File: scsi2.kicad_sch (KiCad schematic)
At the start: 25 parts, among them J3 TO-LED, J4 TO-MB, U4 NCR53c710 SCSI Host Controller, U7 SST39SF010, Y1 Abracon ACO-50MHz

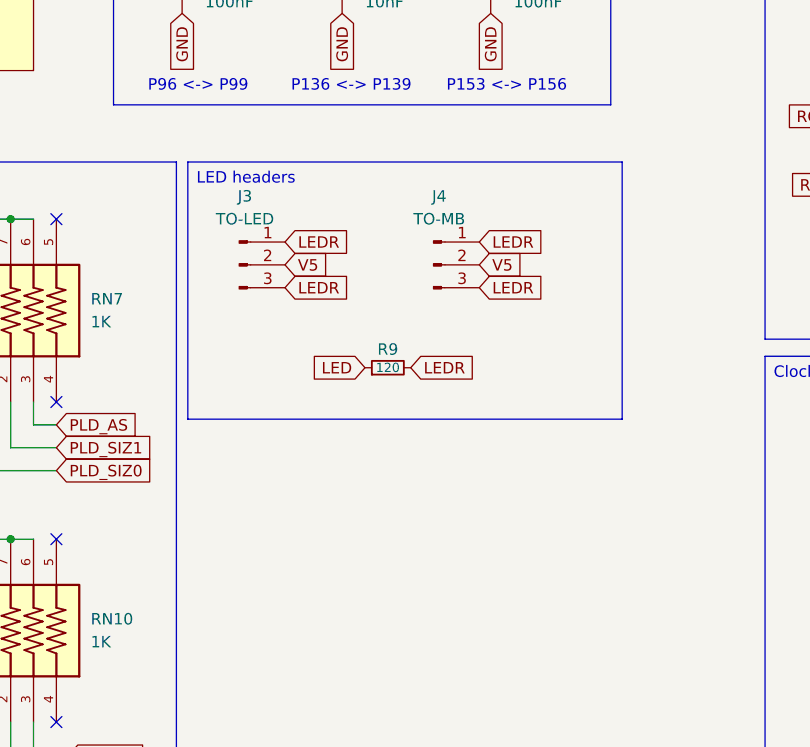
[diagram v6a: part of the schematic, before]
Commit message: Free up some pins and add an LED
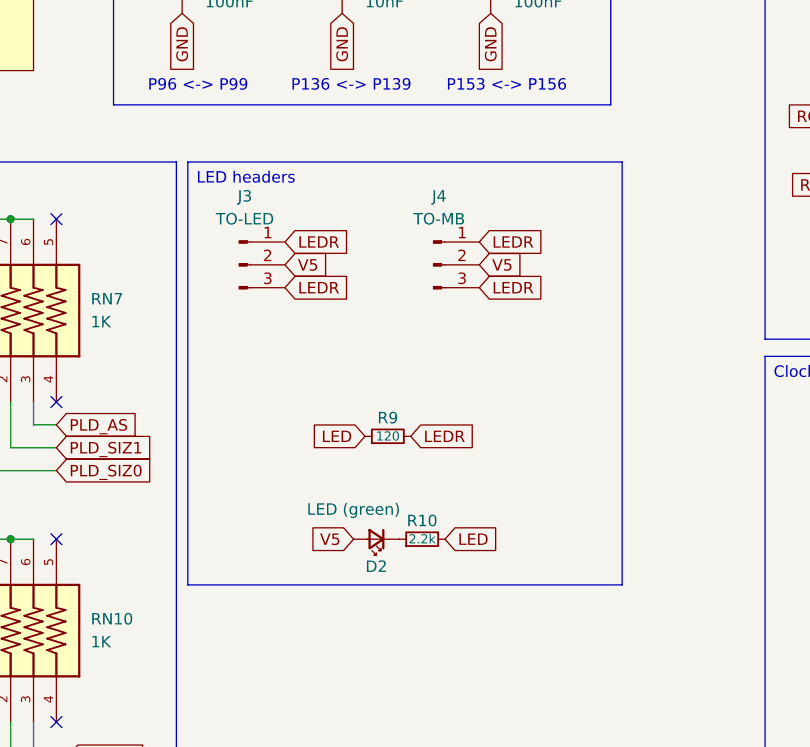
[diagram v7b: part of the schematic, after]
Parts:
- added D2: LED (green), LED_SMD:LED_0805_2012Metric, symbol Device:LED_Small
- added R10: 2.2k, Resistor_SMD:R_0603_1608Metric, symbol Device:R_Small
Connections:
- net LED: now also R10.2
- net V5: now also D2.2 (A)
- new net: D2.1 (K), R10.1
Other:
- moved on the sheet: R9
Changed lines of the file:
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@@
 		(exclude_from_sim no)
 		(at 165.735 86.36 0)
-		(size 48.26 28.575)
+		(size 48.26 46.99)
 		(margins 0.9525 0.9525 0.9525 0.9525)
 		(stroke
@@
 		)
 	)
+	(global_label "V5"
+		(shape input)
+		(at 184.15 128.27 180)
+		(fields_autoplaced yes)
+		(effects
+			(font
+				(size 1.27 1.27)
+			)
+			(justify right)
+		)
+		(property "Intersheetrefs" "${INTERSHEET_REFS}"
+			(at 178.8667 128.27 0)
+			(effects
+				(font
+					(size 1.27 1.27)
+				)
+				(justify right)
+				(hide yes)
+			)
+		)
+	)
 	(global_label "D24"
 		(shape input)
@@
 	(global_label "LEDR"
 		(shape input)
-		(at 190.5 109.22 0)
+		(at 190.5 116.84 0)
 		(fields_autoplaced yes)
 		(effects
@@
 		)
 		(property "Intersheetrefs" "${INTERSHEET_REFS}"
-			(at 198.2023 109.22 0)
+			(at 198.2023 116.84 0)
 			(effects
 				(font
@@
 	(global_label "LED"
 		(shape input)
-		(at 185.42 109.22 180)
+		(at 185.42 116.84 180)
 		(fields_autoplaced yes)
 		(effects
@@
 		)
 		(property "Intersheetrefs" "${INTERSHEET_REFS}"
-			(at 178.9877 109.22 0)
+			(at 178.9877 116.84 0)
 			(effects
 				(font
@@
 		)
 	)
+	(global_label "LED"
+		(shape input)
+		(at 194.31 128.27 0)
+		(fields_autoplaced yes)
+		(effects
+			(font
+				(size 1.27 1.27)
+			)
+			(justify left)
+		)
+		(property "Intersheetrefs" "${INTERSHEET_REFS}"
+			(at 200.7423 128.27 0)
+			(effects
+				(font
+					(size 1.27 1.27)
+				)
+				(justify left)
+				(hide yes)
+			)
+		)
+	)
 	(global_label "A28"
 		(shape input)
@@
 	)
 	(symbol
+		(lib_id "Device:LED_Small")
+		(at 186.69 128.27 180)
+		(unit 1)
+		(exclude_from_sim no)
+		(in_bom yes)
+		(on_board yes)
+		(dnp no)
+		(property "Reference" "D2"
+			(at 186.69 131.318 0)
+			(effects
+				(font
+					(size 1.27 1.27)
+				)
+			)
+		)
+		(property "Value" "LED (green)"
+			(at 184.15 124.968 0)
+			(effects
+				(font
+					(size 1.27 1.27)
+				)
+			)
+		)
+		(property "Footprint" "LED_SMD:LED_0805_2012Metric"
+			(at 186.69 128.27 90)
+			(effects
+				(font
+					(size 1.27 1.27)
+				)
+				(hide yes)
+			)
+		)
+		(property "Datasheet" "~"
+			(at 186.69 128.27 90)
+			(effects
+				(font
+					(size 1.27 1.27)
+				)
+				(hide yes)
+			)
+		)
+		(property "Description" "Light emitting diode, small symbol"
+			(at 186.69 128.27 0)
+			(effects
+				(font
+					(size 1.27 1.27)
+				)
+				(hide yes)
+			)
+		)
+		(property "Sim.Pin" "1=K 2=A"
+			(at 186.69 128.27 0)
+			(effects
+				(font
+					(size 1.27 1.27)
+				)
+				(hide yes)
+			)
+		)
+		(pin "1"
+		)
+		(pin "2"
+		)
+		(instances
+			(project "A4092"
+				(path "/8f9f4021-47aa-41d9-bea7-f6ccf72098bb/2daf4fe3-1e72-4ad5-914a-264df02f69b3"
+					(reference "D2")
+					(unit 1)
+				)
+			)
+		)
+	)
+	(symbol
 		(lib_id "Device:C_Small")
 		(at 165.1 67.31 0)
@@
 	(symbol
 		(lib_id "Device:R_Small")
-		(at 187.96 109.22 90)
+		(at 187.96 116.84 90)
 		(unit 1)
 		(exclude_from_sim no)
@@
 		(dnp no)
 		(property "Reference" "R9"
-			(at 187.96 107.188 90)
+			(at 187.96 114.808 90)
 			(effects
 				(font
@@
 		)
 		(property "Value" "120"
-			(at 187.96 109.22 90)
+			(at 187.96 116.84 90)
 			(effects
 				(font
@@
 		)
 		(property "Footprint" "Resistor_SMD:R_0603_1608Metric"
-			(at 187.96 109.22 0)
+			(at 187.96 116.84 0)
 			(effects
 				(font
@@
 		)
 		(property "Datasheet" "~"
-			(at 187.96 109.22 0)
+			(at 187.96 116.84 0)
 			(effects
 				(font
@@
 		)
 		(property "Description" "Resistor, small symbol"
-			(at 187.96 109.22 0)
+			(at 187.96 116.84 0)
 			(effects
 				(font
@@
 					(unit 1)
 				)
+			)
+		)
+	)
+	(symbol
+		(lib_id "Device:R_Small")
+		(at 191.77 128.27 90)
+		(unit 1)
+		(exclude_from_sim no)
+		(in_bom yes)
+		(on_board yes)
+		(dnp no)
+		(property "Reference" "R10"
+			(at 191.77 126.238 90)
+			(effects
+				(font
+					(size 1.27 1.27)
+				)
+			)
+		)
+		(property "Value" "2.2k"
+			(at 191.77 128.27 90)
+			(effects
+				(font
+					(size 1.016 1.016)
+				)
+			)
+		)
+		(property "Footprint" "Resistor_SMD:R_0603_1608Metric"
+			(at 191.77 128.27 0)
+			(effects
+				(font
+					(size 1.27 1.27)
+				)
+				(hide yes)
+			)
+		)
+		(property "Datasheet" "~"
+			(at 191.77 128.27 0)
+			(effects
+				(font
+					(size 1.27 1.27)
+				)
+				(hide yes)
+			)
+		)
+		(property "Description" "Resistor, small symbol"
+			(at 191.77 128.27 0)
+			(effects
+				(font
+					(size 1.27 1.27)
+				)
+				(hide yes)
+			)
+		)
+		(pin "2"
+		)
+		(pin "1"
+		)
+		(instances
+			(project "A4092"
+				(path "/8f9f4021-47aa-41d9-bea7-f6ccf72098bb/2daf4fe3-1e72-4ad5-914a-264df02f69b3"
+					(reference "R10")
+					(unit 1)
+				)

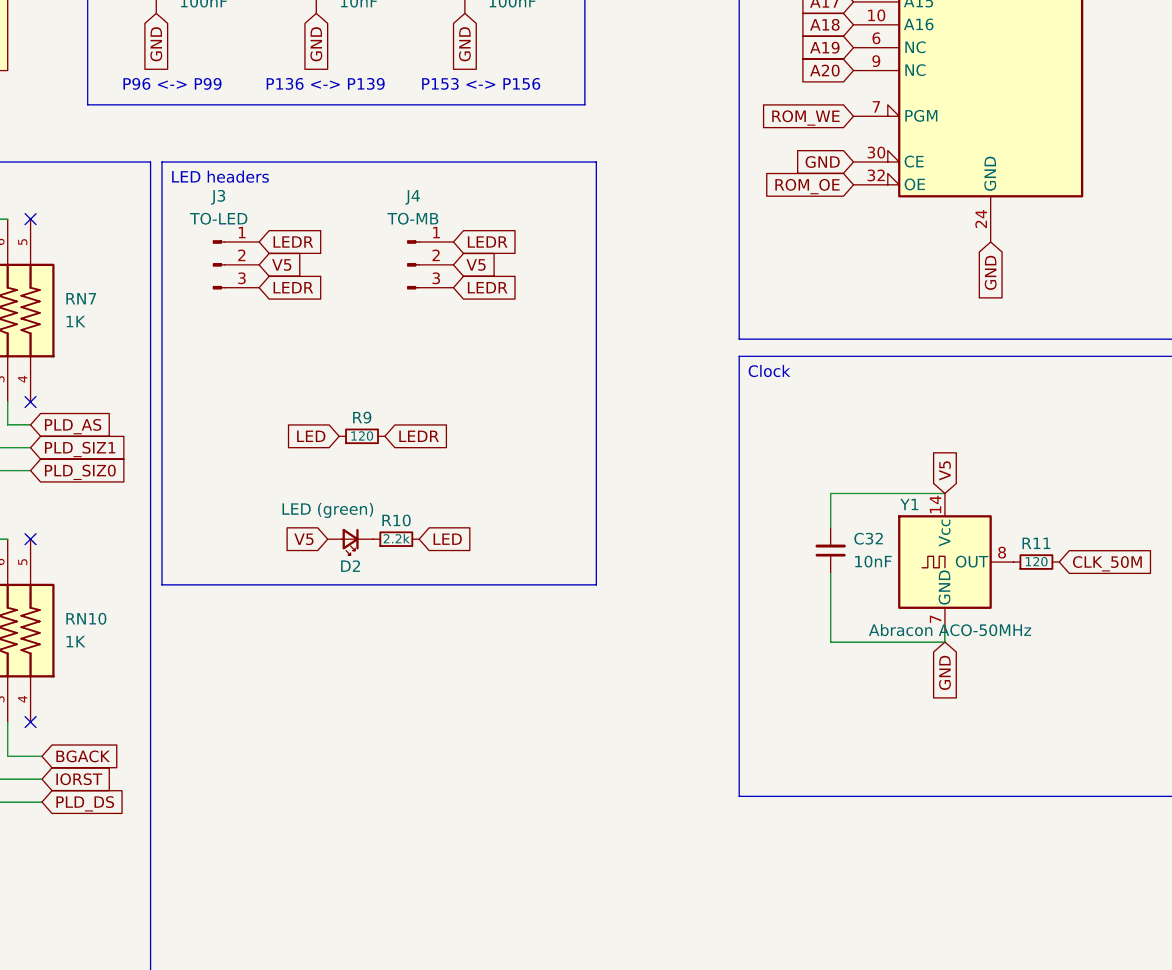
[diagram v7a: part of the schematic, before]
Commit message: Move to XC95144XL
and other changes related to that.
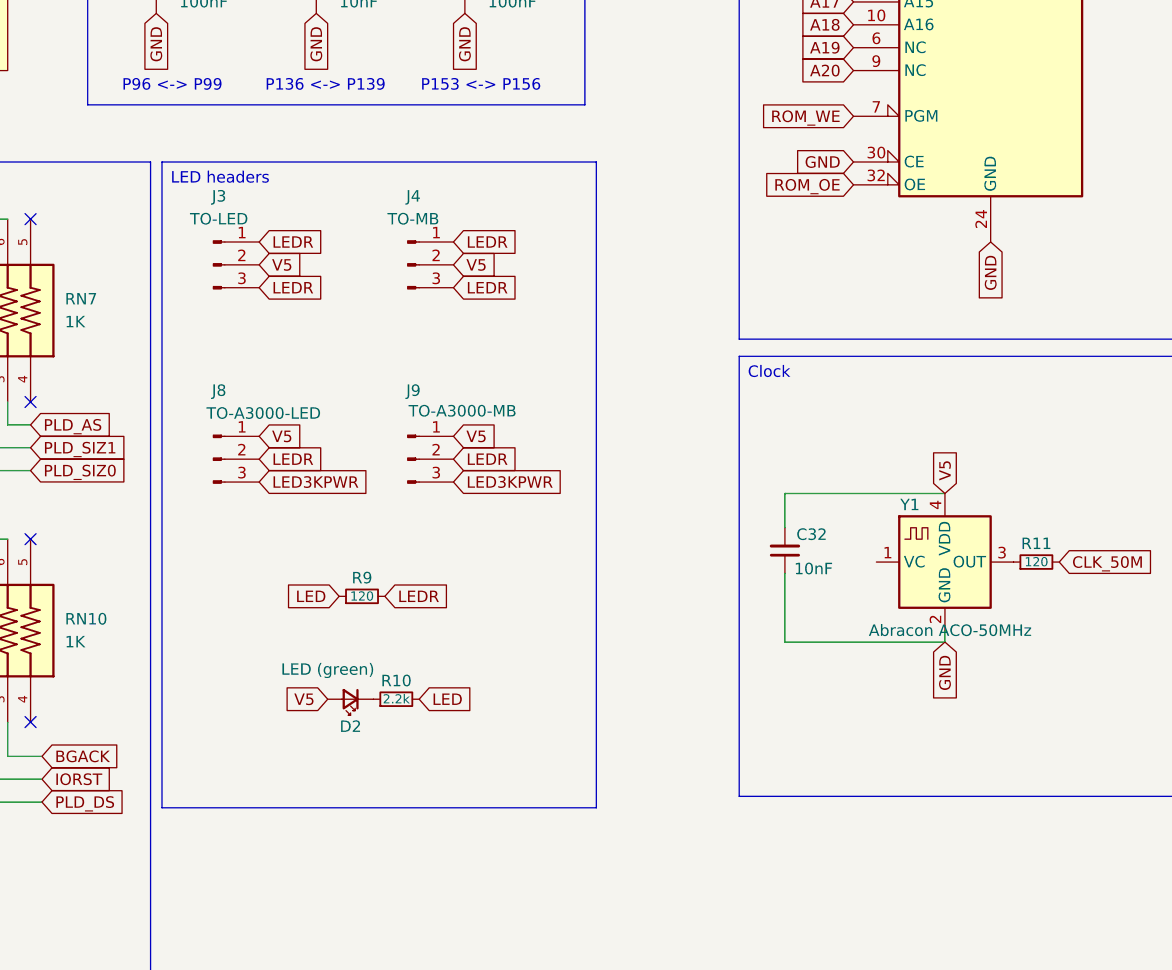
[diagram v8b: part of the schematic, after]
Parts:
- added J8: TO-A3000-LED, Connector_PinHeader_2.54mm:PinHeader_1x03_P2.54mm_Vertical, symbol Connector:Conn_01x03_Pin
- added J9: TO-A3000-MB, Connector_PinHeader_2.54mm:PinHeader_1x03_P2.54mm_Vertical, symbol Connector:Conn_01x03_Pin
- Y1: footprint Oscillator:Oscillator_DIP-14 -> Oscillator:Oscillator_SMD_Fox_FT5H_5.0x3.2mm; symbol Oscillator:ACO-xxxMHz -> Oscillator:FT5HV
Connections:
- net GND: now also Y1.2 (GND); no longer Y1.7 (GND)
- net LEDR: now also J8.2 (Pin_2), J9.2 (Pin_2)
- net V5: now also Y1.4 (VDD), J8.1 (Pin_1), J9.1 (Pin_1); no longer Y1.14 (Vcc)
- net at R11.1: now also Y1.3 (OUT); no longer Y1.8 (OUT)
- new net LED3KPWR: J8.3 (Pin_3), J9.3 (Pin_3)
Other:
- moved on the sheet: C32, D2, R10, R9
